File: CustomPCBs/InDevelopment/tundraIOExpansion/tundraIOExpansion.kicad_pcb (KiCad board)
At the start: 4 copper layers, 46 x 36.5 mm, 56 parts, among them J1 Conn_01x25, J2 Conn_ARM_SWD_TagConnect_TC203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, J3 Conn_ARM_SWD_TagConnect_TC203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, U1 RP2040, U2 MX25L3233FM2, U4 MX25L3233FM2, U5 RP2040, Y1 12.000MHz, Y2 12.000MHz, Y3 32.768kHz

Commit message: tundraIOExpansion ready for DRC
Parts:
- FINGER1, FINGER2, FINGER3, FINGER4, FINGER5L1, FINGER5R1, USB1, USB2: footprint my_connectors:JST_SH_SM04B-SRSS-TB_1x04-1MP_P1.00mm_Horizontal -> Connector_JST:JST_SH_SM04B-SRSS-TB_1x04-1MP_P1.00mm_Horizontal
- FingerAux1: footprint my_connectors:JST_SH_SM08B-SRSS-TB_1x08-1MP_P1.00mm_Horizontal -> Connector_JST:JST_SH_SM08B-SRSS-TB_1x08-1MP_P1.00mm_Horizontal
- moved C8 1.78 mm to (145.9, 83.2)
- moved C25 1.74 mm to (130.5, 83.3)
- moved C26 1.20 mm to (138.4, 73.8)
- moved C6 0.99 mm to (153.6, 74.0)
- moved C4 0.35 mm to (145.2, 82.6)
- moved C22 0.35 mm to (129.8, 82.7)
- moved C21 0.34 mm to (127.9, 83.3)
- moved R7 0.34 mm to (129.2, 82.0)
- moved R2 0.30 mm to (144.6, 81.9)
- moved C12 0.30 mm to (143.3, 83.2)
- moved C27 0.23 mm to (137.7, 73.2)
- turned C11 to -45 degrees
- turned C19 to -45 degrees
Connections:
- C23 pad 1: +1V1 -> Net-(U5-VREG_VOUT)
- C25 pad 1: +1V1 -> Net-(U5-VREG_VOUT)
- C27 pad 1: +1V1 -> Net-(U5-VREG_VOUT)
- C7 pad 1: +1V1 -> Net-(U1-VREG_VOUT)
- C8 pad 1: +1V1 -> Net-(U1-VREG_VOUT)
- C9 pad 1: +1V1 -> Net-(U1-VREG_VOUT)
- U1 pad 23: +1V1 -> Net-(U1-VREG_VOUT)
- U1 pad 45: +1V1 -> Net-(U1-VREG_VOUT)
- U1 pad 50: +1V1 -> Net-(U1-VREG_VOUT)
- U5 pad 23: +1V1 -> Net-(U5-VREG_VOUT)
- U5 pad 45: +1V1 -> Net-(U5-VREG_VOUT)
- U5 pad 50: +1V1 -> Net-(U5-VREG_VOUT)
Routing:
- net INTER_RP2040_UART_TX1: track 0.00 -> 42.6 mm, vias 0 -> 2
- net Net-(FINGER5L1-Pin_2): track 25.8 -> 67.7 mm, vias 2 -> 4
- net INTER_RP2040_UART_RX1: track 0.00 -> 41.7 mm, vias 0 -> 2
- net Net-(FINGER5L1-Pin_3): track 22.9 -> 61.6 mm, vias 0 -> 2
- net +1V1: track 28.6 -> 0.00 mm, vias 2 -> 0
- net Net-(FINGER1-Pin_3): track 0.00 -> 28.5 mm, vias 0 -> 2
- net Net-(FINGER3-Pin_3): track 0.00 -> 25.5 mm, vias 0 -> 2
- net Net-(FINGER3-Pin_2): track 0.00 -> 24.5 mm, vias 0 -> 2
- net Net-(FINGER1-Pin_2): track 0.00 -> 24.1 mm, vias 0 -> 2
- net GND: track 78.8 -> 61.0 mm, vias 31 -> 34
- net Net-(U5-VREG_VOUT): track 0.00 -> 17.5 mm, vias 0 -> 2
- net Net-(U1-VREG_VOUT): track 0.00 -> 17.1 mm, vias 0 -> 2
- net Net-(U1-USB_DM): track 0.00 -> 16.5 mm, vias 0 -> 2
- net Net-(U1-USB_DP): track 0.00 -> 13.5 mm, vias 0 -> 2
- net Net-(U1-QSPI_SS): track 0.00 -> 10.5 mm
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
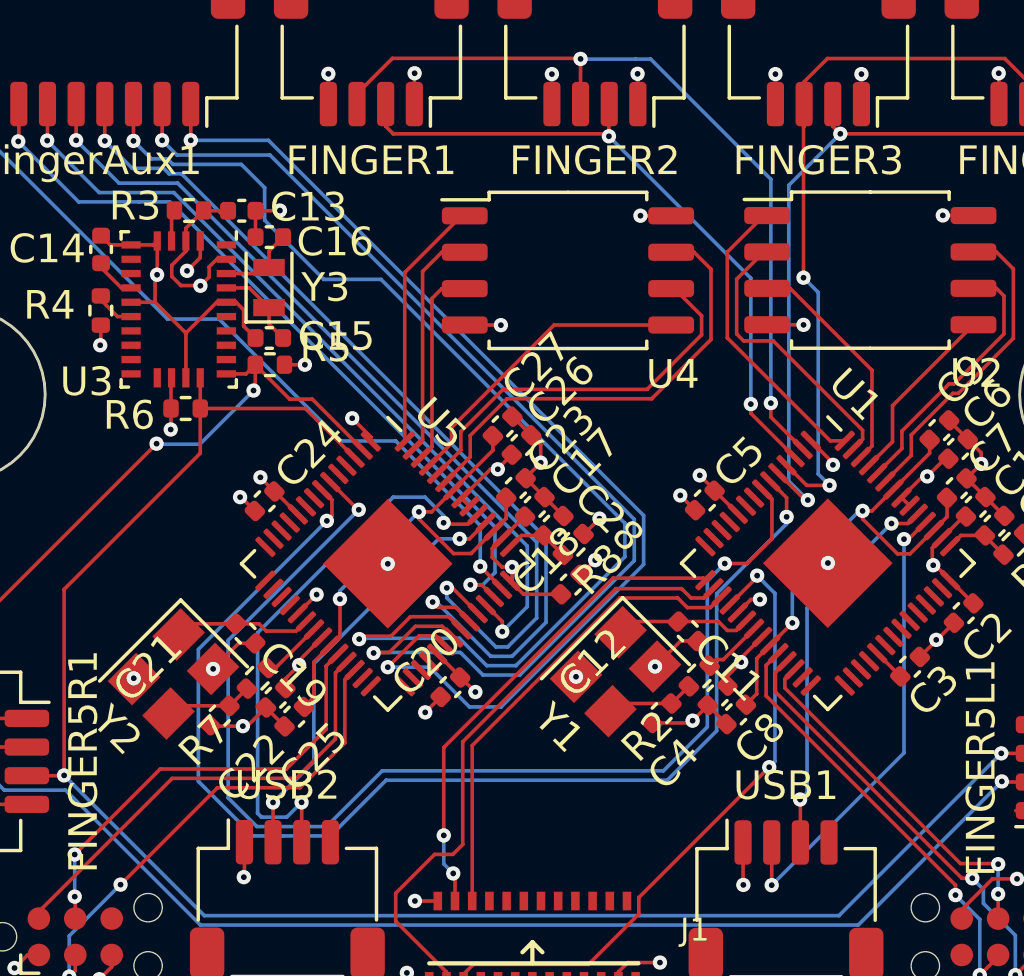
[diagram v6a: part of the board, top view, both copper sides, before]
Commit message: Updating IMU boards for different wire connections
Now all components are placed on one layer, making assembly easier. The
JST connector was dropped for smalled IMU housing, instead the wires now
solder directly to the board and exit from the sides of the board.
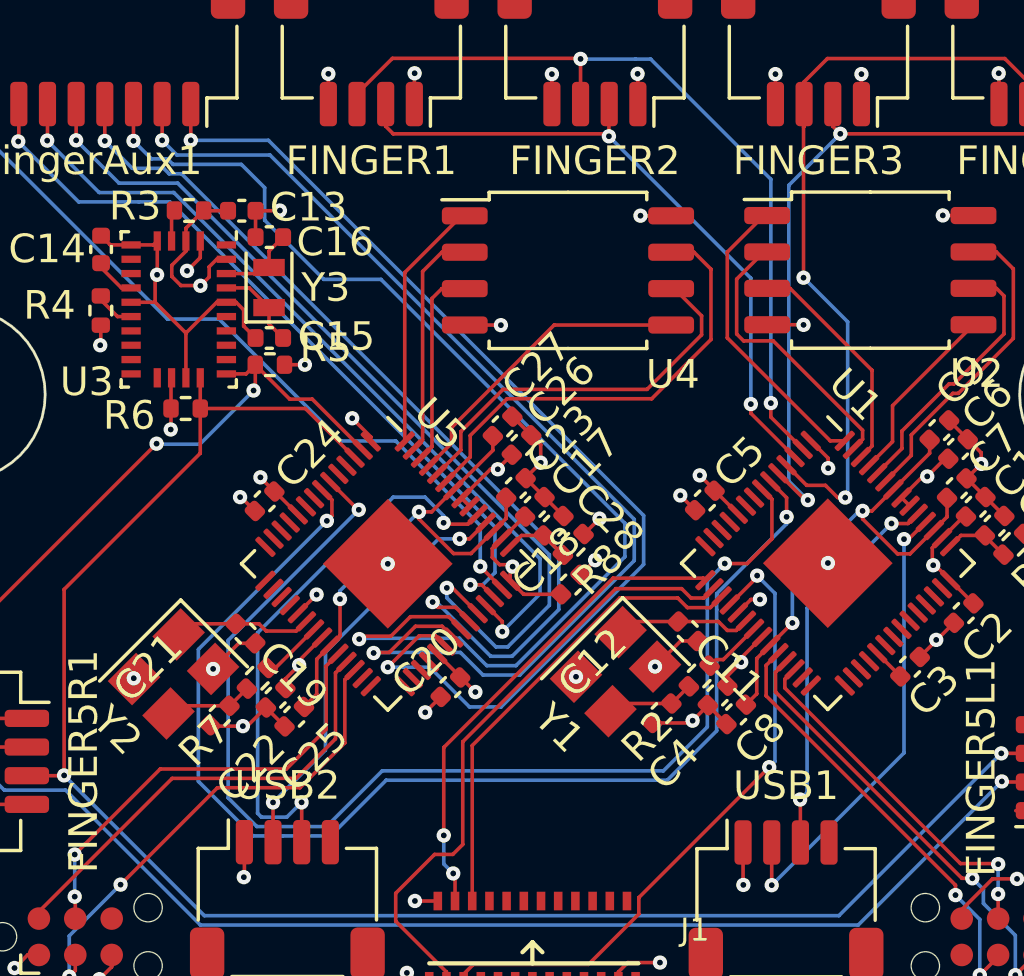
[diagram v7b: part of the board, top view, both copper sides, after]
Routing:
- net Net-(FINGER3-Pin_3): track 25.5 -> 27.0 mm

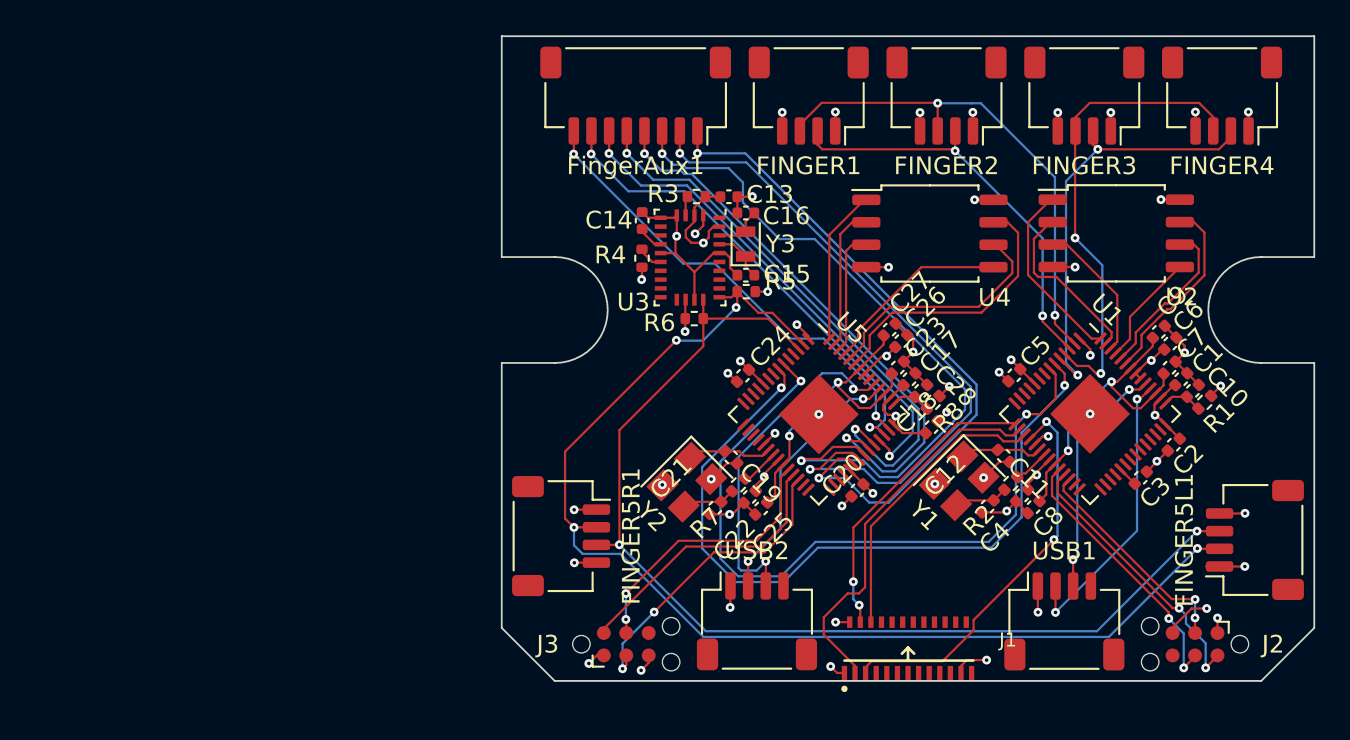
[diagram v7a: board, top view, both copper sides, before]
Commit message: Finished tundra expansion board
Had to add a pull up resistor on QSPI_SS on each RP2040 to enable
BOOT_SEL feature when booting with external jumper/button pressed on
USB, to support booting as external flash storage.
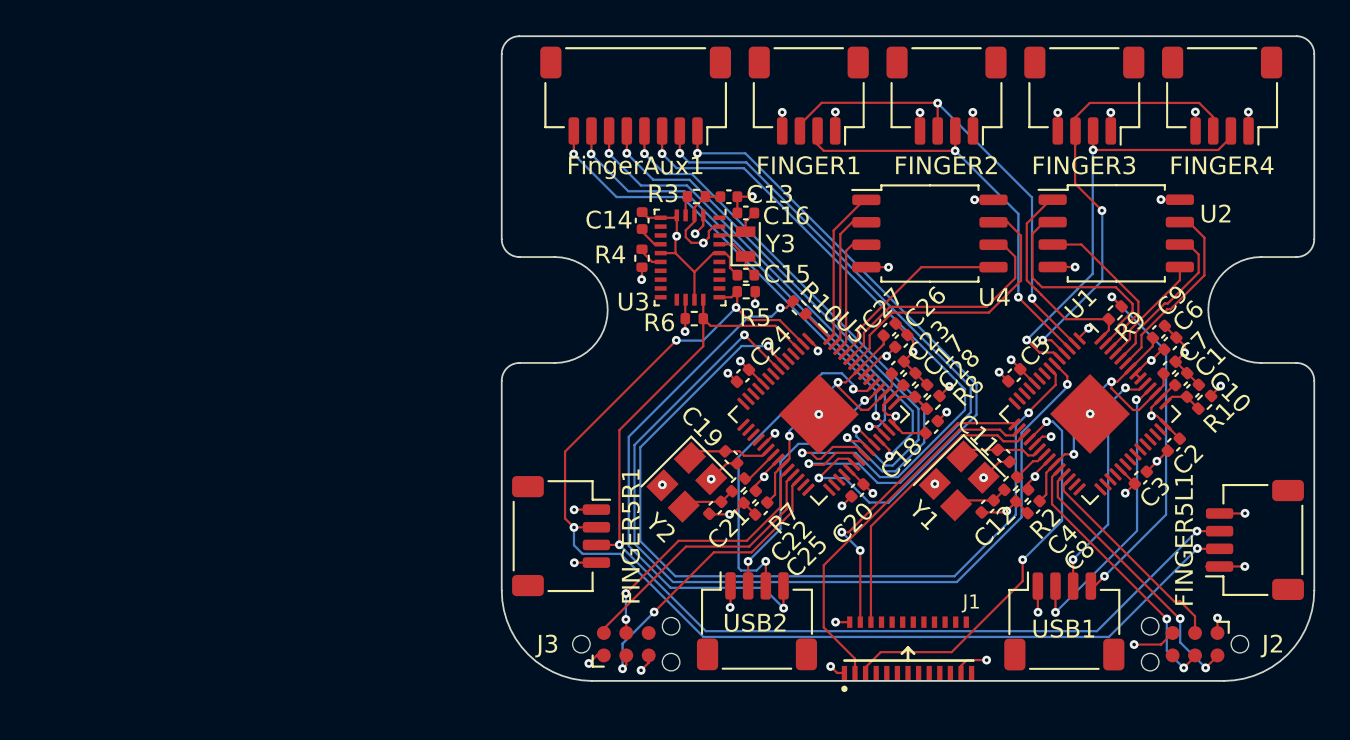
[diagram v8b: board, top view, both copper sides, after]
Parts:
- added R10: 1k, Resistor_SMD:R_0402_1005Metric, F.Cu at (132.6, 72.0)
- added R9: 1k, Resistor_SMD:R_0402_1005Metric, F.Cu at (150.5, 72.2)
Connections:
- USB1 pad 4: VUSB_IN -> Net-(USB1-Pin_4)
- USB2 pad 4: VUSB_IN -> Net-(USB2-Pin_4)
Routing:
- net Net-(USB2-Pin_4): track 0.00 -> 30.1 mm, vias 0 -> 2
- net Net-(USB1-Pin_4): track 0.00 -> 20.3 mm, vias 0 -> 2
- net INTER_RP2040_UART_TX1: track 42.6 -> 51.5 mm
- net INTER_RP2040_UART_RX1: track 41.7 -> 49.2 mm
- net Net-(U1-QSPI_SD1): track 9.95 -> 13.1 mm
- net Net-(U4-~{CS}): track 8.81 -> 10.8 mm
- net Net-(U1-QSPI_SS): track 10.5 -> 12.1 mm
- net Net-(FINGER3-Pin_3): track 27.0 -> 25.5 mm
- net Net-(U1-QSPI_SD2): track 8.03 -> 9.50 mm
- net Net-(FINGER1-Pin_3): track 28.5 -> 27.1 mm
- net D12-MI_MISO: track 17.1 -> 17.9 mm
- net Net-(U4-SCLK): track 13.7 -> 14.4 mm
- net Net-(J2-~{RESET}): track 12.7 -> 12.1 mm, vias 2 -> 0
- net Net-(FingerAux1-Pin_3): track 41.1 -> 40.6 mm
- net +3V3: track 53.1 -> 53.5 mm, vias 28 -> 29
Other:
- outline, holes or cut-outs redrawn
